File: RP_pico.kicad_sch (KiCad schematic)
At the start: 45 parts, among them J17 Conn_01x03_MountingPin, SW1 SW_Push, SW2 SW_Push, U12 W25Q128JVE, U3 RP2350A, Y1 Crystal_GND24

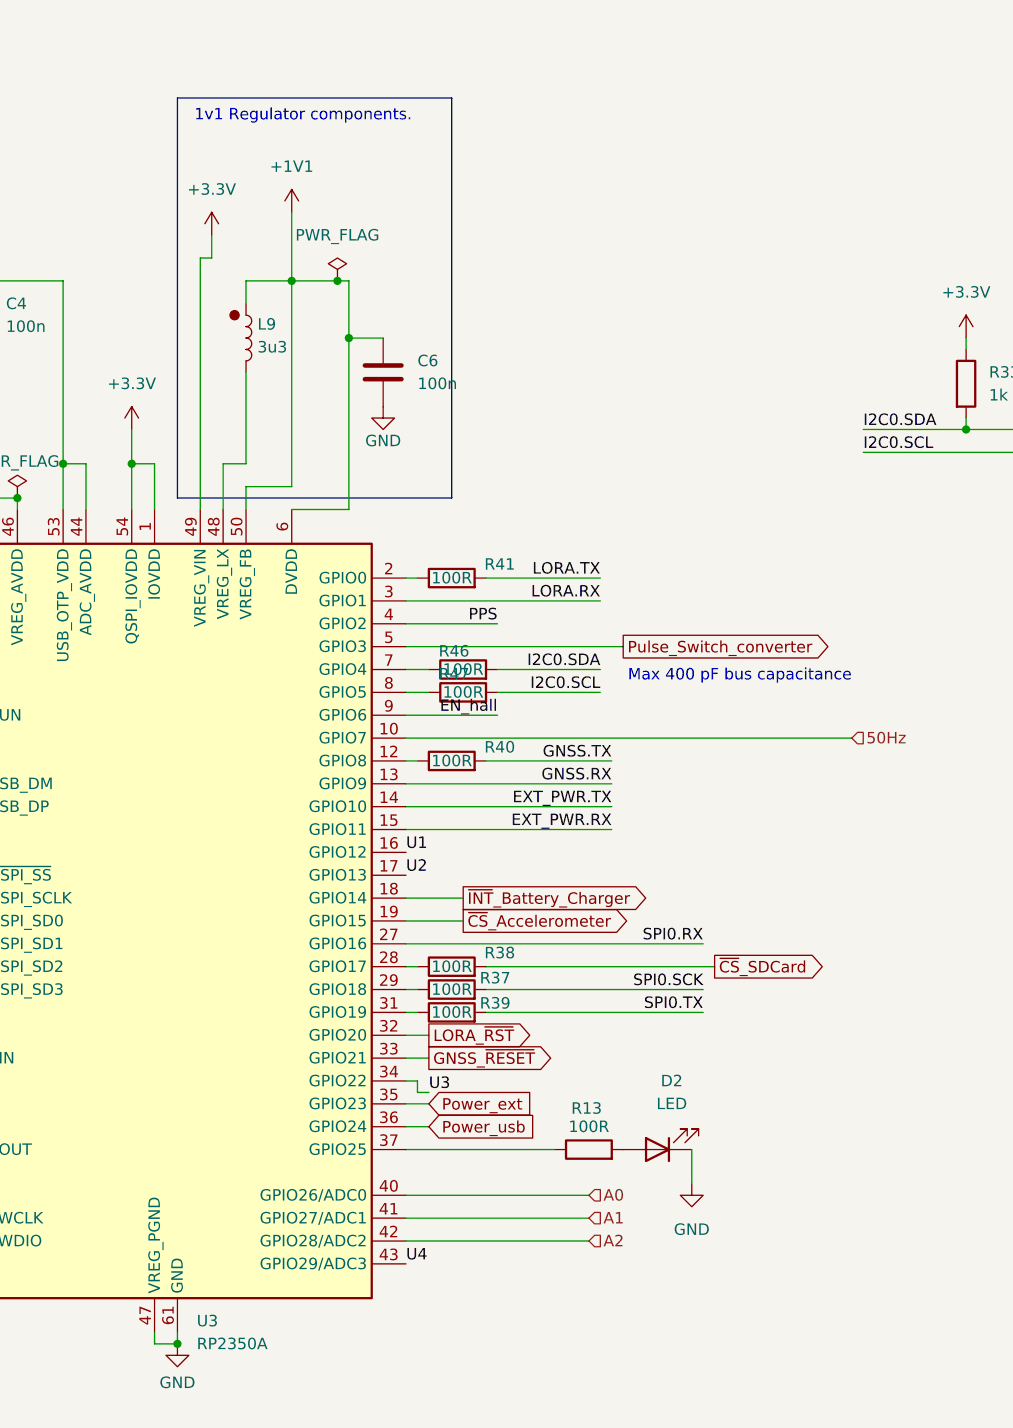
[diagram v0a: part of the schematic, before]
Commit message: PCB routing.
Add netclass flags for power and signal in various schematics; update capacitor footprints and part numbers

- Introduced multiple netclass flags for "Power" and "Signal" in USB_Power, hall_effect_sensor, and nRF9151 schematics to enhance clarity and organization.
- Updated capacitor footprints from "C_1206_3216Metric" to "C_0402_1005Metric" and part numbers from "1206B475K500NT" to "CL05A475MP5NRNC" in accelerometer and nRF9151 schematics for consistency and accuracy.
- Updated submodule reference in kicad-libs to ensure compatibility with the latest library changes.
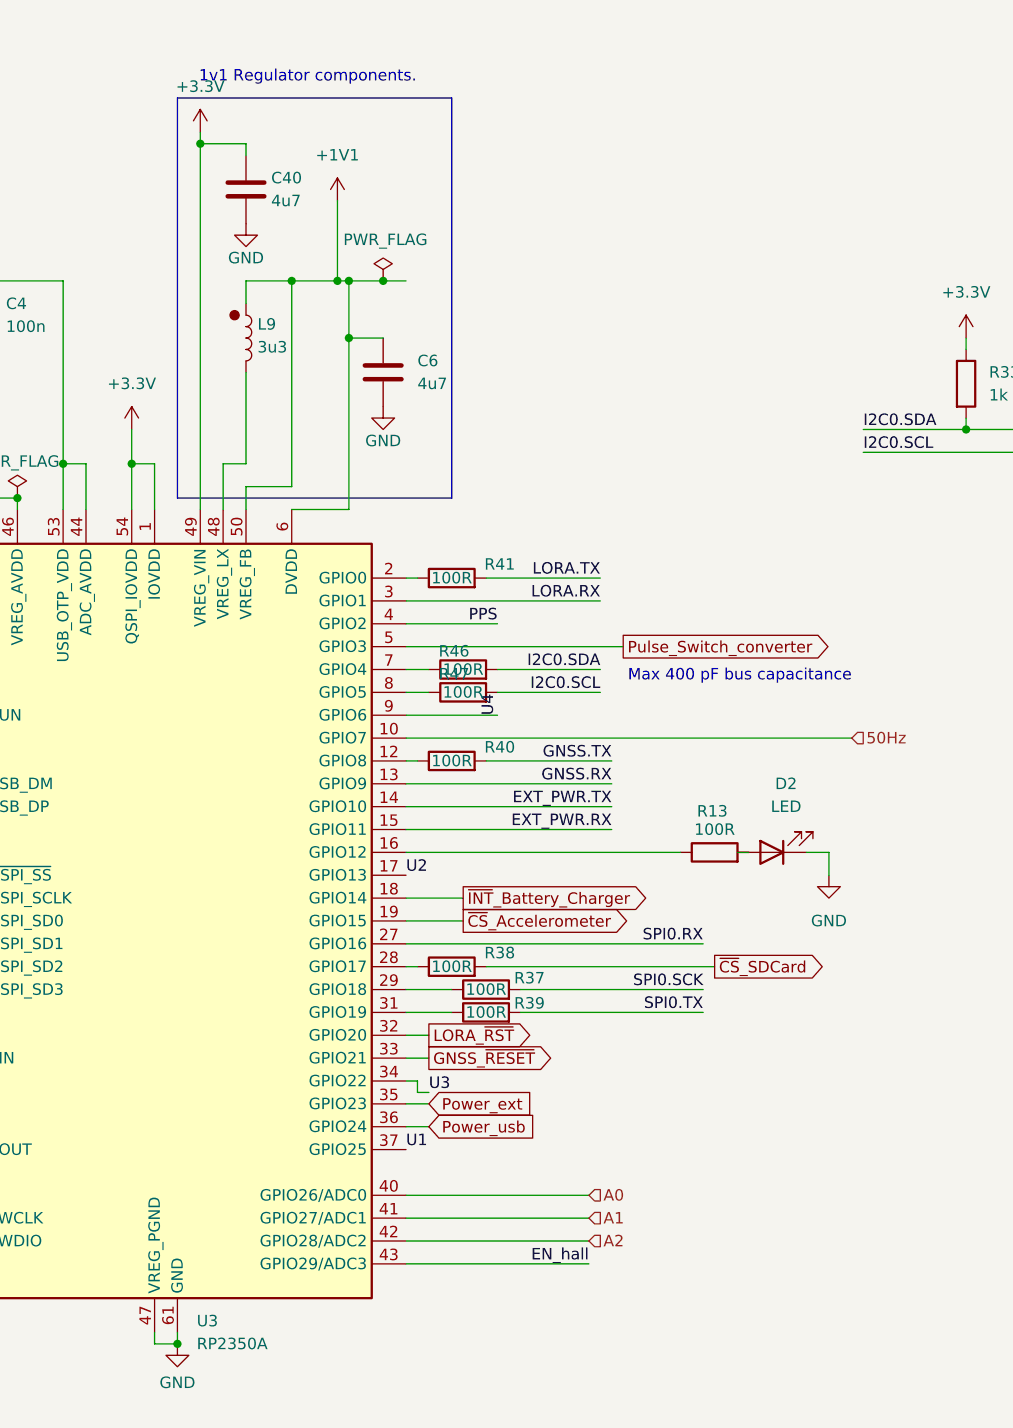
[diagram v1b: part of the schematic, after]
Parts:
- added C40: 4u7, Capacitor_SMD:C_0402_1005Metric, symbol Device:C
- C25, C3: footprint Capacitor_SMD:C_1206_3216Metric -> Capacitor_SMD:C_0402_1005Metric; PartNumber 1206B475K500NT -> CL05A475MP5NRNC
- C6: value 100n -> 4u7; PartNumber CL05B104KO5NNNC -> CL05A475MP5NRNC
- L9: footprint Inductor_SMD:L_0805_2012Metric -> BC_Miscellaneous:AOTA-B201610S3R3-101-T; PartNumber (none) -> AOTA-B201610S3R3-101-T
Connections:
- net +3.3V: now also C40.1
- net EN_hall: now also U3.43 (GPIO29/ADC3); no longer U3.9 (GPIO6)
- net GND: now also C40.2
- net U1: now also U3.37 (GPIO25); no longer U3.16 (GPIO12)
- net U4: now also U3.9 (GPIO6); no longer U3.43 (GPIO29/ADC3)
- net at R13.1: now also U3.16 (GPIO12); no longer U3.37 (GPIO25)
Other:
- moved on the sheet: D2, R13, R37, R39

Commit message: pcb edits. remove old backups
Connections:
- net EN_hall: no longer U3.43 (GPIO29/ADC3)
- new net A3: U3.43 (GPIO29/ADC3)
